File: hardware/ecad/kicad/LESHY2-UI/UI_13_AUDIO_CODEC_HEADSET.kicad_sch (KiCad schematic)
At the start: 0 parts

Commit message: complete exact H2.2.5 audio schematic
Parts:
- added C1: TDK C1005X7R1H104K050BB, Capacitor_SMD:C_0402_1005Metric, symbol Leshy2:UI13_AUDIO_RX_MUX_BYPASS
- added C10: TDK C1608X7R1C105K080AC, Capacitor_SMD:C_0603_1608Metric, symbol Leshy2:UI13_CODEC_ADC_P_COUPLING
- added C11: TDK C1608X7R1C105K080AC, Capacitor_SMD:C_0603_1608Metric, symbol Leshy2:UI13_CODEC_ADC_N_COUPLING
- added C12: TDK C1005X7R1H104K050BB, Capacitor_SMD:C_0402_1005Metric, symbol Leshy2:UI13_AUDIO_SPEAKER_SELECTOR_BYPASS
- added C13: TDK C1005X7R1H104K050BB, Capacitor_SMD:C_0402_1005Metric, symbol Leshy2:UI13_AUDIO_TX_SELECTOR_BYPASS
- added C14: TDK C1608X7R1C105K080AC, Capacitor_SMD:C_0603_1608Metric, symbol Leshy2:UI13_MIC_TX_COUPLING
- added C15: TDK C1608X7R1C105K080AC, Capacitor_SMD:C_0603_1608Metric, symbol Leshy2:UI13_CODEC_TX_COUPLING
- added C16: Murata GRM155R71H103KA88D, Capacitor_SMD:C_0402_1005Metric, symbol Leshy2:UI13_CODEC_TX_FILTER
- added C17: TDK C1005X7R1H104K050BB, Capacitor_SMD:C_0402_1005Metric, symbol Leshy2:UI13_AUDIO_SAFE_GATE_BYPASS
- added C18: Murata GRM188R60J106ME47D, Capacitor_SMD:C_0603_1608Metric, symbol Leshy2:UI13_MICROPHONE_BIAS_FILTER_CAP
- added C19: TDK C1005X7R1H104K050BB, Capacitor_SMD:C_0402_1005Metric, symbol Leshy2:UI13_HEADSET_MIC_SELECTOR_BYPASS
- added C2: TDK C1608X7R1C105K080AC, Capacitor_SMD:C_0603_1608Metric, symbol Leshy2:UI13_AUDIO_VMID_CAP
- added C20: TDK C1005X7R1H104K050BB, Capacitor_SMD:C_0402_1005Metric, symbol Leshy2:UI13_HEADSET_CONTROL_IO_BYPASS
- added C21: Murata GRM21BR60J226ME39L, Capacitor_SMD:C_0805_2012Metric, symbol Leshy2:UI13_HEADPHONE_L_COUPLING0
- added C22: Murata GRM21BR60J226ME39L, Capacitor_SMD:C_0805_2012Metric, symbol Leshy2:UI13_HEADPHONE_L_COUPLING1
- added C23: Murata GRM21BR60J226ME39L, Capacitor_SMD:C_0805_2012Metric, symbol Leshy2:UI13_HEADPHONE_R_COUPLING0
- added C24: Murata GRM21BR60J226ME39L, Capacitor_SMD:C_0805_2012Metric, symbol Leshy2:UI13_HEADPHONE_R_COUPLING1
- added C25: TDK C1608X7R1C105K080AC, Capacitor_SMD:C_0603_1608Metric, symbol Leshy2:UI13_CODEC_POWER_INPUT_CAP
- added C26: Murata GRM188R60J106ME47D, Capacitor_SMD:C_0603_1608Metric, symbol Leshy2:UI13_CODEC_POWER_OUTPUT_CAP
- added C27: TDK C1005X7R1H104K050BB, Capacitor_SMD:C_0402_1005Metric, symbol Leshy2:UI13_CODEC_SUPERVISOR_BYPASS
- added C28: TDK C1005X7R1H104K050BB, Capacitor_SMD:C_0402_1005Metric, symbol Leshy2:UI13_CODEC_I2C_ISO_BYPASS
- added C29: TDK C1005X7R1H104K050BB, Capacitor_SMD:C_0402_1005Metric, symbol Leshy2:UI13_CODEC_I2S_BCLK_ISO_BYPASS
- added C3: TDK C1608X7R1C105K080AC, Capacitor_SMD:C_0603_1608Metric, symbol Leshy2:UI13_VOICE_RX_COUPLING
- added C30: TDK C1005X7R1H104K050BB, Capacitor_SMD:C_0402_1005Metric, symbol Leshy2:UI13_CODEC_I2S_WS_ISO_BYPASS
- added C31: TDK C1005X7R1H104K050BB, Capacitor_SMD:C_0402_1005Metric, symbol Leshy2:UI13_CODEC_I2S_DOUT_ISO_BYPASS
- added C32: TDK C1005X7R1H104K050BB, Capacitor_SMD:C_0402_1005Metric, symbol Leshy2:UI13_CODEC_I2S_DIN_ISO_BYPASS
- added C33: TDK C1005X7R1H104K050BB, Capacitor_SMD:C_0402_1005Metric, symbol Leshy2:UI13_CODEC_I2S_DIN_BOOT_GATE_BYPASS
- added C34: TDK C1005X7R1H104K050BB, Capacitor_SMD:C_0402_1005Metric, symbol Leshy2:UI13_CODEC_PVDD_BYPASS
- added C35: TDK C1005X7R1H104K050BB, Capacitor_SMD:C_0402_1005Metric, symbol Leshy2:UI13_CODEC_DVDD_BYPASS
- added C36: TDK C1005X7R1H104K050BB, Capacitor_SMD:C_0402_1005Metric, symbol Leshy2:UI13_CODEC_AVDD_BYPASS
- added C37: TDK C1608X7R1C105K080AC, Capacitor_SMD:C_0603_1608Metric, symbol Leshy2:UI13_CODEC_DACVREF_CAP
- added C38: TDK C1608X7R1C105K080AC, Capacitor_SMD:C_0603_1608Metric, symbol Leshy2:UI13_CODEC_ADCVREF_CAP
- added C39: TDK C1608X7R1C105K080AC, Capacitor_SMD:C_0603_1608Metric, symbol Leshy2:UI13_CODEC_VMID_CAP
- added C4: TDK C1005X7R1H104K050BB, Capacitor_SMD:C_0402_1005Metric, symbol Leshy2:UI13_AUDIO_CAPTURE_SELECTOR_BYPASS
- added C5: TDK C1608X7R1C105K080AC, Capacitor_SMD:C_0603_1608Metric, symbol Leshy2:UI13_AUDIO_CAPTURE_RX_COUPLING
- added C6: TDK C1608X7R1C105K080AC, Capacitor_SMD:C_0603_1608Metric, symbol Leshy2:UI13_AUDIO_CAPTURE_MIC_COUPLING
- added C7: TDK C1608X7R1C105K080AC, Capacitor_SMD:C_0603_1608Metric, symbol Leshy2:UI13_AUDIO_CAPTURE_INPUT_COUPLING
- added C8: TDK C1608X7R1C105K080AC, Capacitor_SMD:C_0603_1608Metric, symbol Leshy2:UI13_AUDIO_CAPTURE_LOCAL_BIAS_CAP
- added C9: TDK C1005X7R1H104K050BB, Capacitor_SMD:C_0402_1005Metric, symbol Leshy2:UI13_AUDIO_CAPTURE_BUFFER_BYPASS
- added D1: Texas Instruments TPD4E05U06DQAR, Package_SON:USON-10_2.5x1.0mm_P0.5mm, symbol Leshy2:UI13_HEADPHONE_ESD
- added FB1: Murata BLM18PG181SN1D, Inductor_SMD:L_0603_1608Metric, symbol Leshy2:UI13_CODEC_DVDD_BEAD
- added FB2: Murata BLM18PG181SN1D, Inductor_SMD:L_0603_1608Metric, symbol Leshy2:UI13_CODEC_AVDD_BEAD
- added J1: Same Sky SJ-43504-SMT-TR, Leshy2:SJ-43504-SMT-TR, symbol Leshy2:UI13_HEADPHONE_JACK
- added R1: Yageo RC0402FR-0710KL, Resistor_SMD:R_0402_1005Metric, symbol Leshy2:UI13_AUDIO_RX_SEL_PULLDOWN
- added R10: Yageo RC0402FR-07100KL, Resistor_SMD:R_0402_1005Metric, symbol Leshy2:UI13_AUDIO_CAPTURE_LOCAL_BIAS_TOP
- added R11: Yageo RC0402FR-07100KL, Resistor_SMD:R_0402_1005Metric, symbol Leshy2:UI13_AUDIO_CAPTURE_LOCAL_BIAS_BOTTOM
- added R12: Yageo RC0402FR-0733KL, Resistor_SMD:R_0402_1005Metric, symbol Leshy2:UI13_CODEC_ADC_P_SERIES
- added R13: Yageo RC0402FR-0733KL, Resistor_SMD:R_0402_1005Metric, symbol Leshy2:UI13_CODEC_ADC_N_SERIES
- added R14: Yageo RC0402FR-07100KL, Resistor_SMD:R_0402_1005Metric, symbol Leshy2:UI13_MIC_TX_BIAS
- added R15: Yageo RC0402FR-07220KL, Resistor_SMD:R_0402_1005Metric, symbol Leshy2:UI13_CODEC_TX_ATTEN_TOP
- added R16: Yageo RC0402FR-072K2L, Resistor_SMD:R_0402_1005Metric, symbol Leshy2:UI13_CODEC_TX_ATTEN_BOTTOM
- added R17: Yageo RC0402FR-0710KL, Resistor_SMD:R_0402_1005Metric, symbol Leshy2:UI13_AUDIO_SPEAKER_REQ_PULLDOWN
- added R18: Yageo RC0402FR-0710KL, Resistor_SMD:R_0402_1005Metric, symbol Leshy2:UI13_AUDIO_TX_REQ_PULLDOWN
- added R19: Yageo RC0402FR-0710KL, Resistor_SMD:R_0402_1005Metric, symbol Leshy2:UI13_AUDIO_ARM_PULLDOWN
- added R2: Yageo RC0402FR-07100KL, Resistor_SMD:R_0402_1005Metric, symbol Leshy2:UI13_AUDIO_VMID_TOP
- added R20: Yageo RC0402FR-0710KL, Resistor_SMD:R_0402_1005Metric, symbol Leshy2:UI13_AUDIO_SPEAKER_SAFE_PULLDOWN
- added R21: Yageo RC0402FR-0710KL, Resistor_SMD:R_0402_1005Metric, symbol Leshy2:UI13_AUDIO_TX_SAFE_PULLDOWN
- added R22: Yageo RC0402FR-07220RL, Resistor_SMD:R_0402_1005Metric, symbol Leshy2:UI13_MICROPHONE_BIAS_FILTER_RES
- added R23: Yageo RC0402FR-072K2L, Resistor_SMD:R_0402_1005Metric, symbol Leshy2:UI13_MICROPHONE_BIAS_RES
- added R24: Yageo RC0402FR-072K2L, Resistor_SMD:R_0402_1005Metric, symbol Leshy2:UI13_HEADSET_MIC_BIAS_RES
- added R25: Yageo RC0402FR-07100KL, Resistor_SMD:R_0402_1005Metric, symbol Leshy2:UI13_HEADSET_MIC_SELECT_PULLUP
- added R26: Yageo RC0402FR-07100KL, Resistor_SMD:R_0402_1005Metric, symbol Leshy2:UI13_HEADSET_CONTROL_P1_PULLDOWN
- added R27: Yageo RC0402FR-07100KL, Resistor_SMD:R_0402_1005Metric, symbol Leshy2:UI13_HEADSET_CONTROL_P2_PULLDOWN
- added R28: Yageo RC0402FR-07100KL, Resistor_SMD:R_0402_1005Metric, symbol Leshy2:UI13_HEADSET_CONTROL_P3_PULLDOWN
- added R29: Yageo RC0402FR-07100KL, Resistor_SMD:R_0402_1005Metric, symbol Leshy2:UI13_HEADSET_CONTROL_P4_PULLDOWN
- added R3: Yageo RC0402FR-07100KL, Resistor_SMD:R_0402_1005Metric, symbol Leshy2:UI13_AUDIO_VMID_BOTTOM
- added R30: Yageo RC0402FR-07100KL, Resistor_SMD:R_0402_1005Metric, symbol Leshy2:UI13_HEADSET_CONTROL_P5_PULLDOWN
- added R31: Yageo RC0402FR-07100KL, Resistor_SMD:R_0402_1005Metric, symbol Leshy2:UI13_HEADSET_CONTROL_P6_PULLDOWN
- added R32: Yageo RC0402FR-07100KL, Resistor_SMD:R_0402_1005Metric, symbol Leshy2:UI13_HEADSET_CONTROL_P7_PULLDOWN
- added R33: Panasonic ERJ-2RKF22R0X, Resistor_SMD:R_0402_1005Metric, symbol Leshy2:UI13_HEADPHONE_L_SERIES
- added R34: Panasonic ERJ-2RKF22R0X, Resistor_SMD:R_0402_1005Metric, symbol Leshy2:UI13_HEADPHONE_R_SERIES
- added R35: Yageo RC0402FR-0710KL, Resistor_SMD:R_0402_1005Metric, symbol Leshy2:UI13_HEADPHONE_TIP_DETECT_PULLUP
- added R36: Yageo RC0402FR-0710KL, Resistor_SMD:R_0402_1005Metric, symbol Leshy2:UI13_HEADSET_DETECT_SERIES
- added R37: Yageo RC0402FR-07100KL, Resistor_SMD:R_0402_1005Metric, symbol Leshy2:UI13_HEADSET_ABSENT_PULLDOWN
- added R38: Yageo RC0402FR-0710KL, Resistor_SMD:R_0402_1005Metric, symbol Leshy2:UI13_CODEC_POWER_ON_PULLDOWN
- added R39: Yageo RC0402FR-07100KL, Resistor_SMD:R_0402_1005Metric, symbol Leshy2:UI13_CODEC_READY_PULLDOWN
- added R4: Yageo RC0402JR-070RL, Resistor_SMD:R_0402_1005Metric, symbol Leshy2:UI13_AUDIO_GROUND_LINK
- added R40: Yageo RC0402FR-072K2L, Resistor_SMD:R_0402_1005Metric, symbol Leshy2:UI13_CODEC_I2C_SCL_PULLUP
- added R41: Yageo RC0402FR-072K2L, Resistor_SMD:R_0402_1005Metric, symbol Leshy2:UI13_CODEC_I2C_SDA_PULLUP
- added R42: Yageo RC0402FR-0710KL, Resistor_SMD:R_0402_1005Metric, symbol Leshy2:UI13_CODEC_CE_PULLUP
- added R5: Yageo RC0402FR-0710KL, Resistor_SMD:R_0402_1005Metric, symbol Leshy2:UI13_VOICE_RX_SERIES
- added R6: Yageo RC0402FR-07100KL, Resistor_SMD:R_0402_1005Metric, symbol Leshy2:UI13_VOICE_RX_BIAS
- added R7: Yageo RC0402FR-0710KL, Resistor_SMD:R_0402_1005Metric, symbol Leshy2:UI13_AUDIO_CAPTURE_SEL_PULLDOWN
- added R8: Yageo RC0402FR-07100KL, Resistor_SMD:R_0402_1005Metric, symbol Leshy2:UI13_AUDIO_CAPTURE_RX_BIAS
- added R9: Yageo RC0402FR-07100KL, Resistor_SMD:R_0402_1005Metric, symbol Leshy2:UI13_AUDIO_CAPTURE_MIC_BIAS
- added U1: Everest Semiconductor ES8311, Package_DFN_QFN:QFN-20-1EP_3x3mm_P0.4mm_EP1.65x1.65mm, symbol Leshy2:UI13_CODEC
- added U10: Texas Instruments TPS3839K33DBZR, Package_TO_SOT_SMD:SOT-23, symbol Leshy2:UI13_CODEC_SUPERVISOR
- added U11: Texas Instruments SN74LVC2G66DCUR, Package_SO:VSSOP-8_2.3x2mm_P0.5mm, symbol Leshy2:UI13_CODEC_I2C_ISO
- added U12: Texas Instruments SN74LVC1G126DCKR, Package_TO_SOT_SMD:Texas_R-PDSO-G5_DCK-5, symbol Leshy2:UI13_CODEC_I2S_BCLK_ISO
- added U13: Texas Instruments SN74LVC1G126DCKR, Package_TO_SOT_SMD:Texas_R-PDSO-G5_DCK-5, symbol Leshy2:UI13_CODEC_I2S_WS_ISO
- added U14: Texas Instruments SN74LVC1G126DCKR, Package_TO_SOT_SMD:Texas_R-PDSO-G5_DCK-5, symbol Leshy2:UI13_CODEC_I2S_DOUT_ISO
- added U15: Texas Instruments SN74LVC1G126DCKR, Package_TO_SOT_SMD:Texas_R-PDSO-G5_DCK-5, symbol Leshy2:UI13_CODEC_I2S_DIN_ISO
- added U16: SN74LVC1G08DCKR, Package_TO_SOT_SMD:Texas_R-PDSO-G5_DCK-5, symbol Leshy2:UI13_CODEC_I2S_DIN_BOOT_GATE
- added U17: Texas Instruments TPS22919DCKR, Package_TO_SOT_SMD:SOT-363_SC-70-6, symbol Leshy2:UI13_CODEC_POWER_SWITCH
- added U2: Texas Instruments SN74LVC1G3157DBVR, Package_TO_SOT_SMD:SOT-23-6, symbol Leshy2:UI13_AUDIO_RX_MUX
- added U3: Texas Instruments TS5A63157DCKR, Package_TO_SOT_SMD:SOT-363_SC-70-6, symbol Leshy2:UI13_AUDIO_CAPTURE_SELECTOR
- added U4: Texas Instruments TLV9061IDBVR, Package_TO_SOT_SMD:SOT-23-5, symbol Leshy2:UI13_AUDIO_CAPTURE_BUFFER
- added U5: Texas Instruments TMUX1136DGSR, Package_SO:TSSOP-10_3x3mm_P0.5mm, symbol Leshy2:UI13_AUDIO_SPEAKER_SELECTOR
- added U6: Texas Instruments TS5A63157DCKR, Package_TO_SOT_SMD:SOT-363_SC-70-6, symbol Leshy2:UI13_AUDIO_TX_SELECTOR
- added U7: Texas Instruments SN74LVC2G08DCUR, Package_SO:VSSOP-8_2.3x2mm_P0.5mm, symbol Leshy2:UI13_AUDIO_SAFE_GATE
- added U8: Texas Instruments TS5A63157DCKR, Package_TO_SOT_SMD:SOT-363_SC-70-6, symbol Leshy2:UI13_HEADSET_MIC_SELECTOR
- added U9: TCA9534APWR, Package_SO:TSSOP-16_4.4x5mm_P0.65mm, symbol Leshy2:UI13_HEADSET_CONTROL_IO
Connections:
- net 3V3_MAIN: now also C1.1 (END_1), C12.1 (END_1), C13.1 (END_1), C17.1 (END_1), C19.1 (END_1), C20.1 (END_1), C25.1 (END_1), C28.1 (END_1), C29.1 (END_1), C30.1 (END_1), C31.1 (END_1), C32.1 (END_1), C33.1 (END_1), C4.1 (END_1), R2.1 (END_1), R22.1 (END_1), R25.1 (END_1), R35.1 (END_1), U11.8 (VCC), U12.5 (VCC), U13.5 (VCC), U14.5 (VCC), U15.5 (VCC), U16.5 (VCC), U17.1 (IN), U2.5 (VCC), U3.5 (VCC), U5.8 (VDD), U6.5 (VCC), U7.8 (VCC), U8.5 (VCC), U9.1 (A0), U9.16 (VCC)
- net AUDIO_ARM: now also R19.1 (END_1), U16.2 (B), U7.2 (1B), U7.6 (2B)
- net AUDIO_CAPTURE_MIC_SEL: now also R7.1 (END_1), U3.6 (IN)
- net AUDIO_GROUND: now also C1.2 (END_2), C11.1 (END_1), C12.2 (END_2), C13.2 (END_2), C16.2 (END_2), C17.2 (END_2), C18.2 (END_2), C19.2 (END_2), C2.2 (END_2), C20.2 (END_2), C26.2 (END_2), C27.2 (END_2), C34.2 (END_2), C35.2 (END_2), C36.2 (END_2), C37.2 (END_2), C38.2 (END_2), C39.2 (END_2), C4.2 (END_2), C8.2 (END_2), C9.2 (END_2), J1.4 (RING2), R1.2 (END_2), R11.2 (END_2), R17.2 (END_2), R18.2 (END_2), R19.2 (END_2), R20.2 (END_2), R21.2 (END_2), R26.2 (END_2), R27.2 (END_2), R28.2 (END_2), R29.2 (END_2), R3.2 (END_2), R30.2 (END_2), R31.2 (END_2), R32.2 (END_2), R37.2 (END_2), R39.2 (END_2), R4.2 (END_2), R7.2 (END_2), U1.10 (AGND), U1.21 (EPAD), U1.5 (DGND), U10.2 (GND), U2.2 (GND), U3.2 (GND), U4.2 (V_MINUS), U5.3 (GND), U6.2 (GND), U7.4 (GND), U8.2 (GND), U9.2 (A1), U9.3 (A2), U9.8 (GND)
- net AUDIO_SPK_CODEC_REQ: now also R17.1 (END_1), U7.1 (1A)
- net AUDIO_TX_CODEC_REQ: now also R18.1 (END_1), U7.5 (2A)
- net AUDIO_VMID_MAIN: now also C2.1 (END_1), R14.2 (END_2), R16.2 (END_2), R2.2 (END_2), R3.1 (END_1), R6.2 (END_2), R8.2 (END_2), R9.2 (END_2), U5.7 (S2B)
- net CODEC_PWR_EN: now also R38.1 (END_1), U17.3 (ON)
- net HEADSET_ABSENT: now also R36.2 (END_2), R37.1 (END_1)
- net I2S_BCLK: now also U12.2 (A)
- net I2S_DIN: now also U15.4 (Y)
- net I2S_DOUT: now also U14.2 (A)
- net I2S_WS: now also U13.2 (A)
- net MIC_RAW: now also R23.2 (END_2), U8.1 (NO)
- net POWER_GROUND: now also C25.2 (END_2), C28.2 (END_2), C29.2 (END_2), C30.2 (END_2), C31.2 (END_2), C32.2 (END_2), C33.2 (END_2), D1.3 (GND_3), D1.8 (GND_8), R38.2 (END_2), R4.1 (END_1), U11.4 (GND), U12.3 (GND), U13.3 (GND), U14.3 (GND), U15.3 (GND), U16.3 (GND), U17.2 (GND)
- net RX_AUDIO_SOURCE_SEL: now also R1.1 (END_1), U2.6 (S)
- net RX_SA518_AFOUT_ISOLATED: now also C3.1 (END_1)
- net RX_SI4732_MONO: now also U2.3 (B1)
- net SPEAKER_SELECTED_N: now also U5.6 (D2)
- net SPEAKER_SELECTED_P: now also U5.10 (D1)
- net SYS_I2C_SCL: now also U11.5 (2A), U9.14 (SCL)
- net SYS_I2C_SDA: now also U11.1 (1A), U9.15 (SDA)
- net SYS_INT_N: now also U9.13 (INT_N)
- net VOICE_MIC_SELECTED_MAIN: now also U6.4 (COM)
- new net 3V3_CODEC_SWITCHED: C26.1 (END_1), C27.1 (END_1), C34.1 (END_1), C9.1 (END_1), FB1.1 (END_1), FB2.1 (END_1), R10.1 (END_1), R40.1 (END_1), R41.1 (END_1), R42.1 (END_1), U1.3 (PVDD), U10.3 (VDD), U17.5 (QOD), U17.6 (VOUT), U4.5 (V_PLUS)
- new net AUDIO_SPK_SEL_SAFE: R20.1 (END_1), U5.1 (SEL1), U5.5 (SEL2), U7.7 (1Y)
- new net AUDIO_TX_SEL_SAFE: R21.1 (END_1), U6.6 (IN), U7.3 (2Y)
- new net CAPTURE_MIC_BIASED: C6.2 (END_2), R9.1 (END_1), U3.1 (NO)
- new net CAPTURE_RX_BIASED: C5.2 (END_2), R8.1 (END_1), U3.3 (NC)
- new net CAPTURE_SELECTED: C7.1 (END_1), U3.4 (COM)
- new net CODEC_ADCVREF: C38.1 (END_1), U1.15 (ADCVREF)
- new net CODEC_ADC_IN_N: R13.2 (END_2), U1.17 (MIC1N)
- new net CODEC_ADC_IN_P: R12.2 (END_2), U1.18 (MIC1P)
- new net CODEC_ADC_N_AC: C11.2 (END_2), R13.1 (END_1)
- new net CODEC_ADC_P_AC: C10.2 (END_2), R12.1 (END_1)
- new net CODEC_AVDD: C36.1 (END_1), FB2.2 (END_2), U1.11 (AVDD)
- new net CODEC_CAPTURE_BUFFER_FB: C10.1 (END_1), U4.1 (OUT), U4.4 (IN_MINUS)
- new net CODEC_CAPTURE_BUFFER_IN: C7.2 (END_2), C8.1 (END_1), R10.2 (END_2), R11.1 (END_1), U4.3 (IN_PLUS)
- new net CODEC_DACVREF: C37.1 (END_1), U1.14 (DACVREF)
- new net CODEC_DAC_OUT_N: C23.1 (END_1), C24.1 (END_1), U1.13 (OUTN), U5.4 (S2A)
- new net CODEC_DAC_OUT_P: C15.1 (END_1), C21.1 (END_1), C22.1 (END_1), U1.12 (OUTP), U5.2 (S1A)
- new net CODEC_DIN_READY: U15.1 (OE), U16.4 (Y)
- new net CODEC_DVDD: C35.1 (END_1), FB1.2 (END_2), U1.4 (DVDD)
- new net CODEC_I2C_ADDR_0X19: R42.2 (END_2), U1.20 (CE)
- new net CODEC_I2C_SCL: R40.2 (END_2), U1.1 (CCLK), U11.6 (2B)
- new net CODEC_I2C_SDA: R41.2 (END_2), U1.19 (CDATA), U11.2 (1B)
- new net CODEC_I2S_BCLK: U1.6 (SCLK), U12.4 (Y)
- new net CODEC_I2S_DIN_LOCAL: U1.7 (ASDOUT), U15.2 (A)
- new net CODEC_I2S_DOUT: U1.9 (DSDIN), U14.4 (Y)
- new net CODEC_I2S_WS: U1.8 (LRCK), U13.4 (Y)
- new net CODEC_READY: R39.1 (END_1), U10.1 (RESET_N), U11.3 (2C), U11.7 (1C), U12.1 (OE), U13.1 (OE), U14.1 (OE), U16.1 (A)
- new net CODEC_TX_AC: C15.2 (END_2), R15.1 (END_1)
- new net CODEC_VMID: C39.1 (END_1), U1.16 (VMID)
- new net HEADPHONE_LEFT_TIP: D1.1 (D1_PLUS), J1.2 (TIP), R33.2 (END_2), R35.2 (END_2)
- new net HEADPHONE_L_AC: C21.2 (END_2), C22.2 (END_2), R33.1 (END_1)
- new net HEADPHONE_RIGHT_RING1: D1.2 (D1_MINUS), J1.3 (RING1), R34.2 (END_2)
- new net HEADPHONE_R_AC: C23.2 (END_2), C24.2 (END_2), R34.1 (END_1)
- new net HEADSET_INTERNAL_MIC_SEL: R25.2 (END_2), U8.6 (IN), U9.4 (P0)
- new net HEADSET_IO_SPARE_P1: R26.1 (END_1), U9.5 (P1)
- new net HEADSET_IO_SPARE_P2: R27.1 (END_1), U9.6 (P2)
- new net HEADSET_IO_SPARE_P3: R28.1 (END_1), U9.7 (P3)
- new net HEADSET_IO_SPARE_P4: R29.1 (END_1), U9.9 (P4)
- new net HEADSET_IO_SPARE_P5: R30.1 (END_1), U9.10 (P5)
- new net HEADSET_IO_SPARE_P6: R31.1 (END_1), U9.11 (P6)
- new net HEADSET_IO_SPARE_P7: R32.1 (END_1), U9.12 (P7)
- new net HEADSET_MIC_RAW: D1.4 (D2_PLUS), J1.1 (SLEEVE), R24.2 (END_2), U8.3 (NC)
- new net HEADSET_SWITCH_STATE: J1.5 (TIP_SWITCH), R36.1 (END_1)
- new net MIC_BIAS_FILTERED: C18.1 (END_1), R22.2 (END_2), R23.1 (END_1), R24.1 (END_1)
- new net MIC_SELECTED_RAW: C14.1 (END_1), C6.1 (END_1), U8.4 (COM)
- new net RX_AUDIO_SELECTED: C5.1 (END_1), U2.4 (A_COM), U5.9 (S1B)
- new net RX_SA518_AFOUT_AC: C3.2 (END_2), R5.1 (END_1)
- new net RX_SA518_AFOUT_BIASED: R5.2 (END_2), R6.1 (END_1), U2.1 (B2)
- new net VOICE_CODEC_INJECT: C16.1 (END_1), R15.2 (END_2), R16.1 (END_1), U6.1 (NO)
- new net VOICE_ELECTRET_DEFAULT: C14.2 (END_2), R14.1 (END_1), U6.3 (NC)
- no-connect marks 24 -> 8
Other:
- title: (none) -> Leshy2 — exact codec, capture, playback and CTIA headset

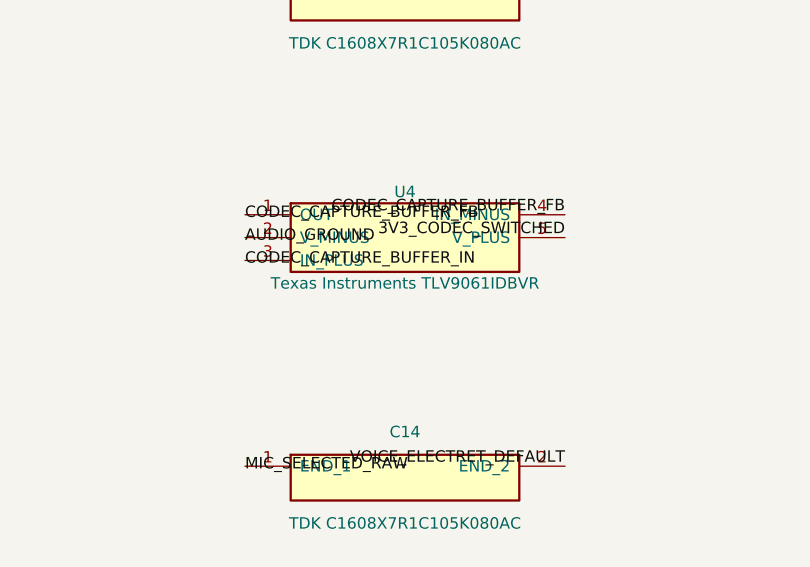
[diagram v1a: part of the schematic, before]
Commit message: complete exact H2.2.9 UI TX safety schematic
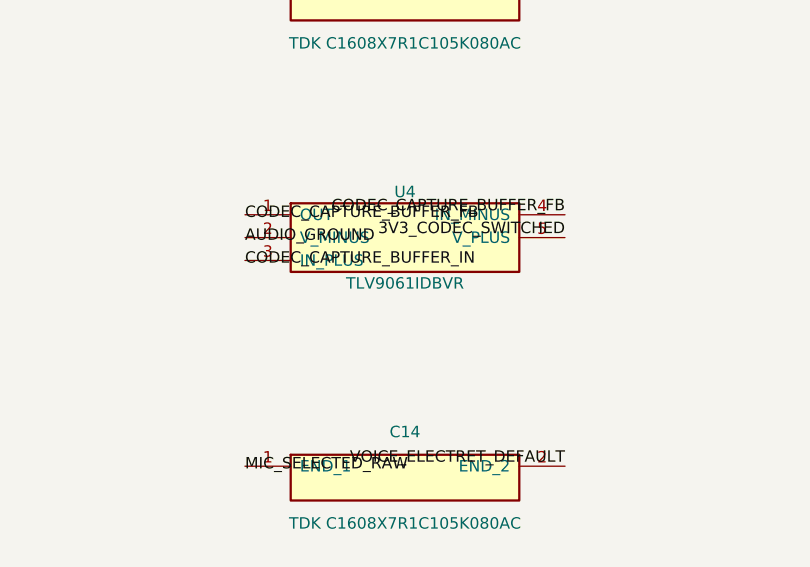
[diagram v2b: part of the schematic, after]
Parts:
- U4: value Texas Instruments TLV9061IDBVR -> TLV9061IDBVR
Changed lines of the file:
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@@
 			(effects (font (size 1.27 1.27)))
 		)
-		(property "Value" "Texas Instruments TLV9061IDBVR"
+		(property "Value" "TLV9061IDBVR"
 			(at 294.64 127.00 0)
 			(show_name no)

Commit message: complete H2 schematic review package
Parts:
- renumbered C1 to C13001, C2 to C13002, C3 to C13003, C4 to C13004, C5 to C13005, C6 to C13006, C7 to C13007, C8 to C13008, C9 to C13009, C10 to C13010, C11 to C13011, C12 to C13012, C13 to C13013, C14 to C13014, C15 to C13015, C16 to C13016, C17 to C13017, C18 to C13018, C19 to C13019, C20 to C13020, C21 to C13021, C22 to C13022, C23 to C13023, C24 to C13024, C25 to C13025, C26 to C13026, C27 to C13027, C28 to C13028, C29 to C13029, C30 to C13030, C31 to C13031, C32 to C13032, C33 to C13033, C34 to C13034, C35 to C13035, C36 to C13036, C37 to C13037, C38 to C13038, C39 to C13039, D1 to D13001, FB1 to FB13001, FB2 to FB13002, J1 to J13001, R1 to R13001, R2 to R13002, R3 to R13003, R4 to R13004, R5 to R13005, R6 to R13006, R7 to R13007, R8 to R13008, R9 to R13009, R10 to R13010, R11 to R13011, R12 to R13012, R13 to R13013, R14 to R13014, R15 to R13015, R16 to R13016, R17 to R13017, R18 to R13018, R19 to R13019, R20 to R13020, R21 to R13021, R22 to R13022, R23 to R13023, R24 to R13024, R25 to R13025, R26 to R13026, R27 to R13027, R28 to R13028, R29 to R13029, R30 to R13030, R31 to R13031, R32 to R13032, R33 to R13033, R34 to R13034, R35 to R13035, R36 to R13036, R37 to R13037, R38 to R13038, R39 to R13039, R40 to R13040, R41 to R13041, R42 to R13042, U1 to U13001, U2 to U13002, U3 to U13003, U4 to U13004, U5 to U13005, U6 to U13006, U7 to U13007, U8 to U13008, U9 to U13009, U10 to U13010, U11 to U13011, U12 to U13012, U13 to U13013, U14 to U13014, U15 to U13015, U16 to U13016, U17 to U13017

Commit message: Verify H3.3.2 audio electrical corners
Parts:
- added C13020: Murata GRM188R60J106ME47D, Capacitor_SMD:C_0603_1608Metric, symbol Leshy2:UI13_HEADSET_MICROPHONE_BIAS_FILTER_CAP
- added R13024: Yageo RC0402FR-07220RL, Resistor_SMD:R_0402_1005Metric, symbol Leshy2:UI13_HEADSET_MICROPHONE_BIAS_FILTER_RES
- R13012, R13013: value Yageo RC0402FR-0733KL -> Yageo RC0402JR-070RL
- R13015: value Yageo RC0402FR-07220KL -> Vishay CRCW0402160KFKED
- renumbered C13020 to C13021, C13021 to C13022, C13022 to C13023, C13023 to C13024, C13024 to C13025, C13025 to C13026, C13026 to C13027, C13027 to C13028, C13028 to C13029, C13029 to C13030, C13030 to C13031, C13031 to C13032, C13032 to C13033, C13033 to C13034, C13034 to C13035, C13035 to C13036, C13036 to C13037, C13037 to C13038, C13038 to C13039, C13039 to C13040, R13024 to R13025, R13025 to R13026, R13026 to R13027, R13027 to R13028, R13028 to R13029, R13029 to R13030, R13030 to R13031, R13031 to R13032, R13032 to R13033, R13033 to R13034, R13034 to R13035, R13035 to R13036, R13036 to R13037, R13037 to R13038, R13038 to R13039, R13039 to R13040, R13040 to R13041, R13041 to R13042, R13042 to R13043
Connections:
- net 3V3_MAIN: now also R13024.1 (END_1)
- net AUDIO_GROUND: now also C13020.2 (END_2)
- net MIC_BIAS_FILTERED: no longer R13025.1 (END_1)
- new net HEADSET_MIC_BIAS_FILTERED: C13020.1 (END_1), R13024.2 (END_2), R13025.1 (END_1)
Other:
- moved on the sheet: C13021, C13022, C13023, C13024, C13025, C13026, C13027, C13028, C13029, C13030, C13031, C13032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

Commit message: Reclose H2 through H4 on dual SA818S architecture
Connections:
- net RX_SA518_AFOUT_AC renamed RX_VOICE_AFOUT_AC
- net RX_SA518_AFOUT_BIASED renamed RX_VOICE_AFOUT_BIASED
- net RX_SA518_AFOUT_ISOLATED renamed RX_VOICE_AFOUT_SELECTED
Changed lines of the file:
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@@
-		(effects (font (size 1.27 1.27)))
-	)
-	(label "RX_SA518_AFOUT_AC"
-		(at 312.42 68.58 180)
-		(effects (font (size 1.27 1.27)) (justify right bottom))
-	)
-	(label "RX_SA518_AFOUT_AC"
-		(at 358.14 68.58 0)
-		(effects (font (size 1.27 1.27)))
-	)
-	(label "RX_SA518_AFOUT_BIASED"
-		(at 114.30 43.18 0)
-		(effects (font (size 1.27 1.27)))
-	)
-	(label "RX_SA518_AFOUT_BIASED"
-		(at 393.70 68.58 180)
-		(effects (font (size 1.27 1.27)) (justify right bottom))
-	)
-	(label "RX_SA518_AFOUT_BIASED"
-		(at 439.42 68.58 0)
-		(effects (font (size 1.27 1.27)))
-	)
-	(hierarchical_label "RX_SA518_AFOUT_ISOLATED"
-		(shape bidirectional)
-		(at 276.86 68.58 0)
 		(effects (font (size 1.27 1.27)))
 	)
@@
 		(effects (font (size 1.27 1.27)))
 	)
+	(label "RX_VOICE_AFOUT_AC"
+		(at 312.42 68.58 180)
+		(effects (font (size 1.27 1.27)) (justify right bottom))
+	)
+	(label "RX_VOICE_AFOUT_AC"
+		(at 358.14 68.58 0)
+		(effects (font (size 1.27 1.27)))
+	)
+	(label "RX_VOICE_AFOUT_BIASED"
+		(at 114.30 43.18 0)
+		(effects (font (size 1.27 1.27)))
+	)
+	(label "RX_VOICE_AFOUT_BIASED"
+		(at 393.70 68.58 180)
+		(effects (font (size 1.27 1.27)) (justify right bottom))
+	)
+	(label "RX_VOICE_AFOUT_BIASED"
+		(at 439.42 68.58 0)
+		(effects (font (size 1.27 1.27)))
+	)
+	(hierarchical_label "RX_VOICE_AFOUT_SELECTED"
+		(shape bidirectional)
+		(at 276.86 68.58 0)
+		(effects (font (size 1.27 1.27)))
+	)

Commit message: Optimize H1 display and stocked BOM routes
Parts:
- C13001, C13004, C13009, C13012, C13013, C13017, C13019, C13021, C13028, C13029, C13030, C13031, C13032, C13033, C13034, C13035, C13036, C13037: value TDK C1005X7R1H104K050BB -> Yageo CC0402KRX7R9BB104
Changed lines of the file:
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@@
 			(effects (font (size 1.27 1.27)))
 		)
-		(property "Value" "TDK C1005X7R1H104K050BB"
+		(property "Value" "Yageo CC0402KRX7R9BB104"
 			(at 213.36 49.53 0)
 			(show_name no)
@@
 			(effects (font (size 1.27 1.27)))
 		)
-		(property "Value" "TDK C1005X7R1H104K050BB"
+		(property "Value" "Yageo CC0402KRX7R9BB104"
 			(at 132.08 77.47 0)
 			(show_name no)
@@
 			(effects (font (size 1.27 1.27)))
 		)
-		(property "Value" "TDK C1005X7R1H104K050BB"
+		(property "Value" "Yageo CC0402KRX7R9BB104"
 			(at 375.92 125.73 0)
 			(show_name no)
@@
 			(effects (font (size 1.27 1.27)))
 		)
-		(property "Value" "TDK C1005X7R1H104K050BB"
+		(property "Value" "Yageo CC0402KRX7R9BB104"
 			(at 375.92 151.13 0)
 			(show_name no)
@@
 			(effects (font (size 1.27 1.27)))
 		)
-		(property "Value" "TDK C1005X7R1H104K050BB"
+		(property "Value" "Yageo CC0402KRX7R9BB104"
 			(at 132.08 153.67 0)
 			(show_name no)
@@
 			(effects (font (size 1.27 1.27)))
 		)
-		(property "Value" "TDK C1005X7R1H104K050BB"
+		(property "Value" "Yageo CC0402KRX7R9BB104"
 			(at 538.48 179.07 0)
 			(show_name no)
@@
 			(effects (font (size 1.27 1.27)))
 		)
-		(property "Value" "TDK C1005X7R1H104K050BB"
+		(property "Value" "Yageo CC0402KRX7R9BB104"
 			(at 132.08 229.87 0)
 			(show_name no)
@@
 			(effects (font (size 1.27 1.27)))
 		)
-		(property "Value" "TDK C1005X7R1H104K050BB"
+		(property "Value" "Yageo CC0402KRX7R9BB104"
 			(at 50.80 255.27 0)
 			(show_name no)
@@
 			(effects (font (size 1.27 1.27)))
 		)
-		(property "Value" "TDK C1005X7R1H104K050BB"
+		(property "Value" "Yageo CC0402KRX7R9BB104"
 			(at 457.20 331.47 0)
 			(show_name no)
@@
 			(effects (font (size 1.27 1.27)))
 		)
-		(property "Value" "TDK C1005X7R1H104K050BB"
+		(property "Value" "Yageo CC0402KRX7R9BB104"
 			(at 375.92 339.09 0)
 			(show_name no)
@@
 			(effects (font (size 1.27 1.27)))
 		)
-		(property "Value" "TDK C1005X7R1H104K050BB"
+		(property "Value" "Yageo CC0402KRX7R9BB104"
 			(at 294.64 377.19 0)
 			(show_name no)
@@
 			(effects (font (size 1.27 1.27)))
 		)
-		(property "Value" "TDK C1005X7R1H104K050BB"
+		(property "Value" "Yageo CC0402KRX7R9BB104"
 			(at 50.80 382.27 0)
 			(show_name no)
@@
 			(effects (font (size 1.27 1.27)))
 		)
-		(property "Value" "TDK C1005X7R1H104K050BB"
+		(property "Value" "Yageo CC0402KRX7R9BB104"
 			(at 132.08 384.81 0)
 			(show_name no)
@@
 			(effects (font (size 1.27 1.27)))
 		)
-		(property "Value" "TDK C1005X7R1H104K050BB"
+		(property "Value" "Yageo CC0402KRX7R9BB104"
 			(at 457.20 384.81 0)
 			(show_name no)
@@
 			(effects (font (size 1.27 1.27)))
 		)
-		(property "Value" "TDK C1005X7R1H104K050BB"
+		(property "Value" "Yageo CC0402KRX7R9BB104"
 			(at 538.48 384.81 0)
 			(show_name no)
@@
 			(effects (font (size 1.27 1.27)))
 		)
-		(property "Value" "TDK C1005X7R1H104K050BB"
+		(property "Value" "Yageo CC0402KRX7R9BB104"
 			(at 375.92 392.43 0)
 			(show_name no)
@@
 			(effects (font (size 1.27 1.27)))
 		)
-		(property "Value" "TDK C1005X7R1H104K050BB"
+		(property "Value" "Yageo CC0402KRX7R9BB104"
 			(at 294.64 402.59 0)
 			(show_name no)
@@
 			(effects (font (size 1.27 1.27)))
 		)
-		(property "Value" "TDK C1005X7R1H104K050BB"
+		(property "Value" "Yageo CC0402KRX7R9BB104"
 			(at 132.08 410.21 0)
 			(show_name no)

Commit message: Replace six pre-order resistor identities
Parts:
- R13016, R13023, R13025, R13041, R13042: value Yageo RC0402FR-072K2L -> UNI-ROYAL 0402WGF2201TCE
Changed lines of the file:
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@@
 			(effects (font (size 1.27 1.27)))
 		)
-		(property "Value" "Yageo RC0402FR-072K2L"
+		(property "Value" "UNI-ROYAL 0402WGF2201TCE"
 			(at 457.20 179.07 0)
 			(show_name no)
@@
 			(effects (font (size 1.27 1.27)))
 		)
-		(property "Value" "Yageo RC0402FR-072K2L"
+		(property "Value" "UNI-ROYAL 0402WGF2201TCE"
 			(at 213.36 209.55 0)
 			(show_name no)
@@
 			(effects (font (size 1.27 1.27)))
 		)
-		(property "Value" "Yageo RC0402FR-072K2L"
+		(property "Value" "UNI-ROYAL 0402WGF2201TCE"
 			(at 213.36 234.95 0)
 			(show_name no)
@@
 			(effects (font (size 1.27 1.27)))
 		)
-		(property "Value" "Yageo RC0402FR-072K2L"
+		(property "Value" "UNI-ROYAL 0402WGF2201TCE"
 			(at 294.64 351.79 0)
 			(show_name no)
@@
 			(effects (font (size 1.27 1.27)))
 		)
-		(property "Value" "Yageo RC0402FR-072K2L"
+		(property "Value" "UNI-ROYAL 0402WGF2201TCE"
 			(at 50.80 356.87 0)
 			(show_name no)

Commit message: Replace three pre-order passive parts
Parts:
- R13015: value Vishay CRCW0402160KFKED -> UNI-ROYAL 0402WGF1603TCE
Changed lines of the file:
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@@
 			(effects (font (size 1.27 1.27)))
 		)
-		(property "Value" "Vishay CRCW0402160KFKED"
+		(property "Value" "UNI-ROYAL 0402WGF1603TCE"
 			(at 375.92 176.53 0)
 			(show_name no)
